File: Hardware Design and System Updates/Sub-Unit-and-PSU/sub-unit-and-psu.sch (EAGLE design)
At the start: 15 parts, among them U1 BA033CC0FP-E2TO252-3_ROM, U2 MSP430FR2000IPW16PW16_TEX, U3 TLR342F-GE2SOP8_ROM, U4 TMP36GT9ZT_3_ADI

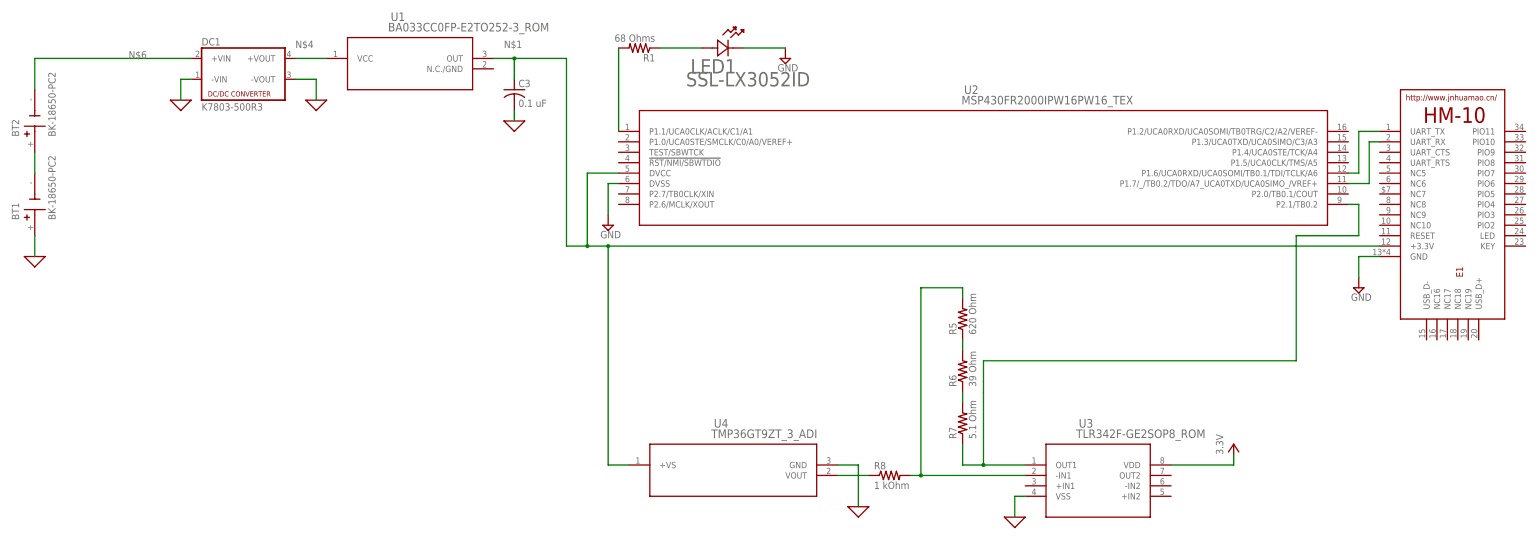
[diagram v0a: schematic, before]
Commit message: Added 5v regulator to schematics
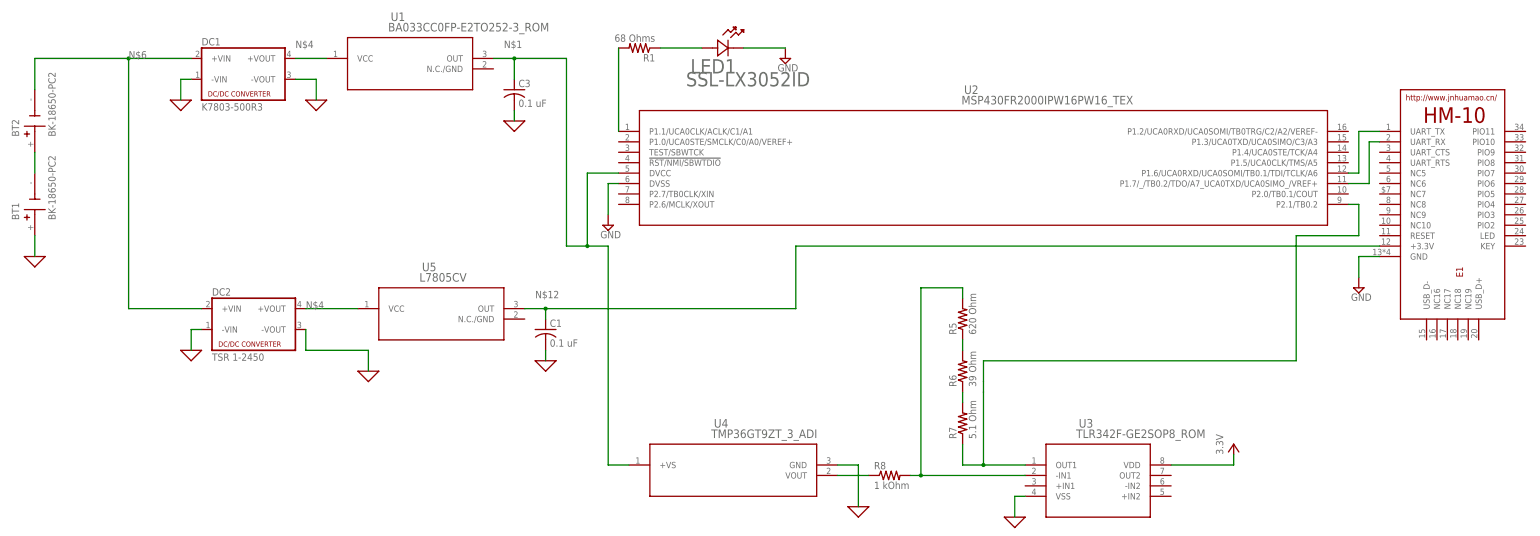
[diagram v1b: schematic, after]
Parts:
- added C1: 0.1 uF, rcl:C-US050-024X044
- added DC2: TSR 1-2450, dc-dc-converter:NME
- added U5: L7805CV, 2023-03-08_12-17-23_Library:BA033CC0FP-E2TO252-3_ROM
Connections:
- new net N$12: C1.1, E1.+3.3V, U5.OUT
- net 0: now also C1.2, DC2.-VIN, DC2.-VOUT
- net N$1: no longer E1.+3.3V
- net N$4: now also DC2.+VOUT, U5.VCC
- net N$6: now also DC2.+VIN
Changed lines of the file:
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@@
 <part name="U4" library="2023-03-28_14-12-25_Library" deviceset="TMP36GT9Z" device="T_3_ADI"/>
 <part name="X_3" library="ngspice-simulation" library_urn="urn:adsk.eagle:library:527439" deviceset="GND" device=""/>
+<part name="DC2" library="dc-dc-converter" library_urn="urn:adsk.eagle:library:208" deviceset="NME" device="" package3d_urn="urn:adsk.eagle:package:12313/1" value="TSR 1-2450"/>
+<part name="X_5" library="ngspice-simulation" library_urn="urn:adsk.eagle:library:527439" deviceset="GND" device=""/>
+<part name="U5" library="2023-03-08_12-17-23_Library" deviceset="BA033CC0FP-E2" device="TO252-3_ROM" value="L7805CV"/>
+<part name="X_8" library="ngspice-simulation" library_urn="urn:adsk.eagle:library:527439" deviceset="GND" device=""/>
+<part name="C1" library="rcl" library_urn="urn:adsk.eagle:library:334" deviceset="C-US" device="050-024X044" package3d_urn="urn:adsk.eagle:package:23643/1" value="0.1 uF"/>
+<part name="X_7" library="ngspice-simulation" library_urn="urn:adsk.eagle:library:527439" deviceset="GND" device=""/>
 </parts>
 <sheets>
@@
 </instance>
 <instance part="X_3" gate="G$1" x="317.5" y="40.64" smashed="yes"/>
+<instance part="DC2" gate="G$1" x="170.18" y="86.36" smashed="yes">
+<attribute name="NAME" x="160.02" y="92.075" size="1.778" layer="95"/>
+<attribute name="VALUE" x="160.02" y="76.2" size="1.778" layer="96"/>
+</instance>
+<instance part="X_5" gate="G$1" x="154.94" y="78.74" smashed="yes"/>
+<instance part="U5" gate="A" x="193.04" y="88.9" smashed="yes">
+<attribute name="NAME" x="211.1746" y="98.0186" size="2.083" layer="95" ratio="6"/>
+<attribute name="VALUE" x="210.5352" y="95.4786" size="2.083" layer="96" ratio="6"/>
+</instance>
+<instance part="X_8" gate="G$1" x="198.12" y="73.66" smashed="yes"/>
+<instance part="C1" gate="G$1" x="241.3" y="83.82" smashed="yes">
+<attribute name="NAME" x="242.316" y="84.455" size="1.778" layer="95"/>
+<attribute name="VALUE" x="242.316" y="79.629" size="1.778" layer="96"/>
+</instance>
+<instance part="X_7" gate="G$1" x="241.3" y="76.2" smashed="yes"/>
 </instances>
 <busses>
@@
 <pinref part="X_3" gate="G$1" pin="0"/>
 </segment>
+<segment>
+<pinref part="X_5" gate="G$1" pin="0"/>
+<pinref part="DC2" gate="G$1" pin="-VIN"/>
+<wire x1="154.94" y1="78.74" x2="154.94" y2="83.82" width="0.1524" layer="91"/>
+<wire x1="154.94" y1="83.82" x2="157.48" y2="83.82" width="0.1524" layer="91"/>
+</segment>
+<segment>
+<pinref part="DC2" gate="G$1" pin="-VOUT"/>
+<wire x1="182.88" y1="83.82" x2="182.88" y2="78.74" width="0.1524" layer="91"/>
+<wire x1="182.88" y1="78.74" x2="198.12" y2="78.74" width="0.1524" layer="91"/>
+<pinref part="X_8" gate="G$1" pin="0"/>
+<wire x1="198.12" y1="73.66" x2="198.12" y2="78.74" width="0.1524" layer="91"/>
+</segment>
+<segment>
+<pinref part="X_7" gate="G$1" pin="0"/>
+<pinref part="C1" gate="G$1" pin="2"/>
+<wire x1="241.3" y1="76.2" x2="241.3" y2="78.74" width="0.1524" layer="91"/>
+</segment>
 </net>
 <net name="N$4" class="0">
@@
 <pinref part="U1" gate="A" pin="VCC"/>
 </segment>
-</net>
-<net name="N$6" class="0">
-<segment>
-<pinref part="DC1" gate="G$1" pin="+VIN"/>
-<wire x1="116.84" y1="149.86" x2="154.94" y2="149.86" width="0.1524" layer="91"/>
-<label x="139.7" y="149.86" size="1.778" layer="95"/>
-<pinref part="BT2" gate="G$1" pin="-"/>
-<wire x1="116.84" y1="142.24" x2="116.84" y2="149.86" width="0.1524" layer="91"/>
+<segment>
+<pinref part="DC2" gate="G$1" pin="+VOUT"/>
+<wire x1="182.88" y1="88.9" x2="195.58" y2="88.9" width="0.1524" layer="91"/>
+<label x="182.88" y="88.9" size="1.778" layer="95"/>
+<pinref part="U5" gate="A" pin="VCC"/>
 </segment>
 </net>
@@
 <wire x1="259.08" y1="121.92" x2="251.46" y2="121.92" width="0.1524" layer="91"/>
 <wire x1="251.46" y1="121.92" x2="251.46" y2="104.14" width="0.1524" layer="91"/>
-<pinref part="E1" gate="G$1" pin="+3.3V"/>
 <wire x1="251.46" y1="104.14" x2="256.54" y2="104.14" width="0.1524" layer="91"/>
 <junction x="251.46" y="104.14"/>
-<wire x1="256.54" y1="104.14" x2="444.5" y2="104.14" width="0.1524" layer="91"/>
 <wire x1="251.46" y1="104.14" x2="246.38" y2="104.14" width="0.1524" layer="91"/>
 <wire x1="228.6" y1="149.86" x2="233.68" y2="149.86" width="0.1524" layer="91"/>
@@
 <wire x1="261.62" y1="50.8" x2="256.54" y2="50.8" width="0.1524" layer="91"/>
 <wire x1="256.54" y1="50.8" x2="256.54" y2="104.14" width="0.1524" layer="91"/>
-<junction x="256.54" y="104.14"/>
 </segment>
 </net>
@@
 </segment>
 </net>
+<net name="N$12" class="0">
+<segment>
+<wire x1="236.22" y1="88.9" x2="241.3" y2="88.9" width="0.1524" layer="91"/>
+<label x="238.76" y="91.44" size="1.778" layer="95"/>
+<pinref part="U5" gate="A" pin="OUT"/>
+<pinref part="C1" gate="G$1" pin="1"/>
+<wire x1="241.3" y1="86.36" x2="241.3" y2="88.9" width="0.1524" layer="91"/>
+<junction x="241.3" y="88.9"/>
+<wire x1="241.3" y1="88.9" x2="302.26" y2="88.9" width="0.1524" layer="91"/>
+<pinref part="E1" gate="G$1" pin="+3.3V"/>
+<wire x1="444.5" y1="104.14" x2="302.26" y2="104.14" width="0.1524" layer="91"/>
+<wire x1="302.26" y1="104.14" x2="302.26" y2="88.9" width="0.1524" layer="91"/>
+</segment>
+</net>
+<net name="N$6" class="0">
+<segment>
+<pinref part="DC2" gate="G$1" pin="+VIN"/>
+<wire x1="139.7" y1="88.9" x2="157.48" y2="88.9" width="0.1524" layer="91"/>
+<pinref part="DC1" gate="G$1" pin="+VIN"/>
+<wire x1="116.84" y1="149.86" x2="139.7" y2="149.86" width="0.1524" layer="91"/>
+<label x="139.7" y="149.86" size="1.778" layer="95"/>
+<pinref part="BT2" gate="G$1" pin="-"/>
+<wire x1="139.7" y1="149.86" x2="154.94" y2="149.86" width="0.1524" layer="91"/>
+<wire x1="116.84" y1="142.24" x2="116.84" y2="149.86" width="0.1524" layer="91"/>
+<wire x1="139.7" y1="88.9" x2="139.7" y2="149.86" width="0.1524" layer="91"/>
+<junction x="139.7" y="149.86"/>
+</segment>
+</net>

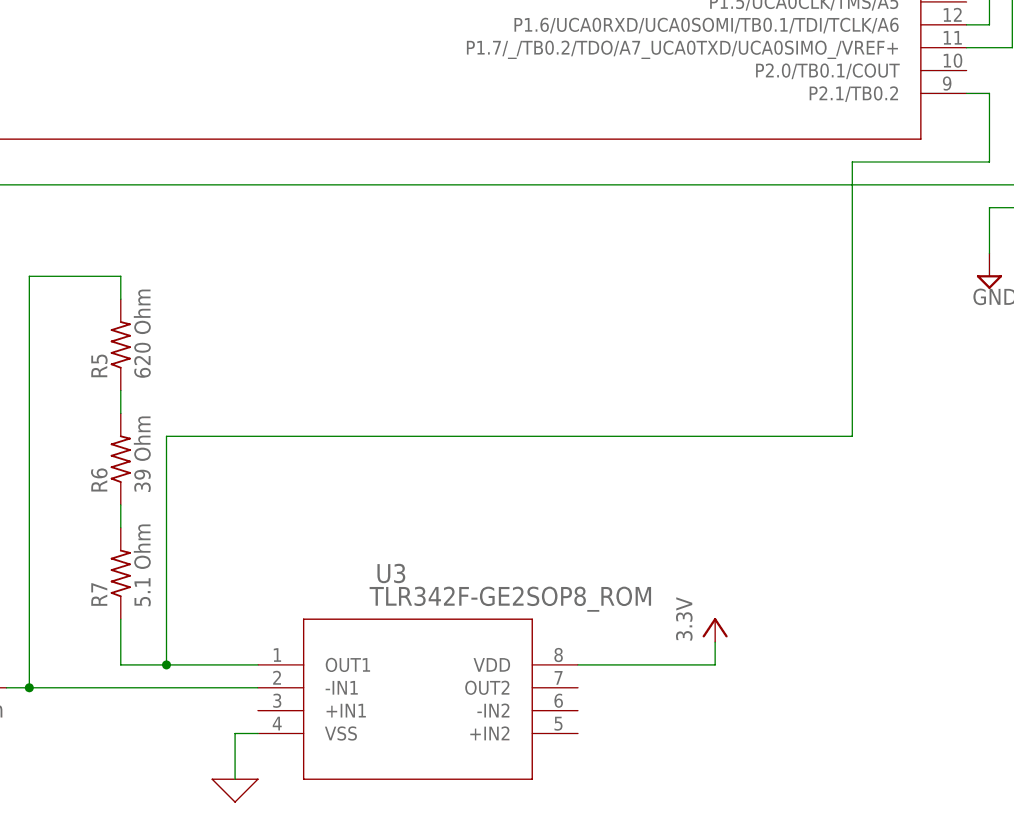
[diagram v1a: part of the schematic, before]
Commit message: Fixed system schematics
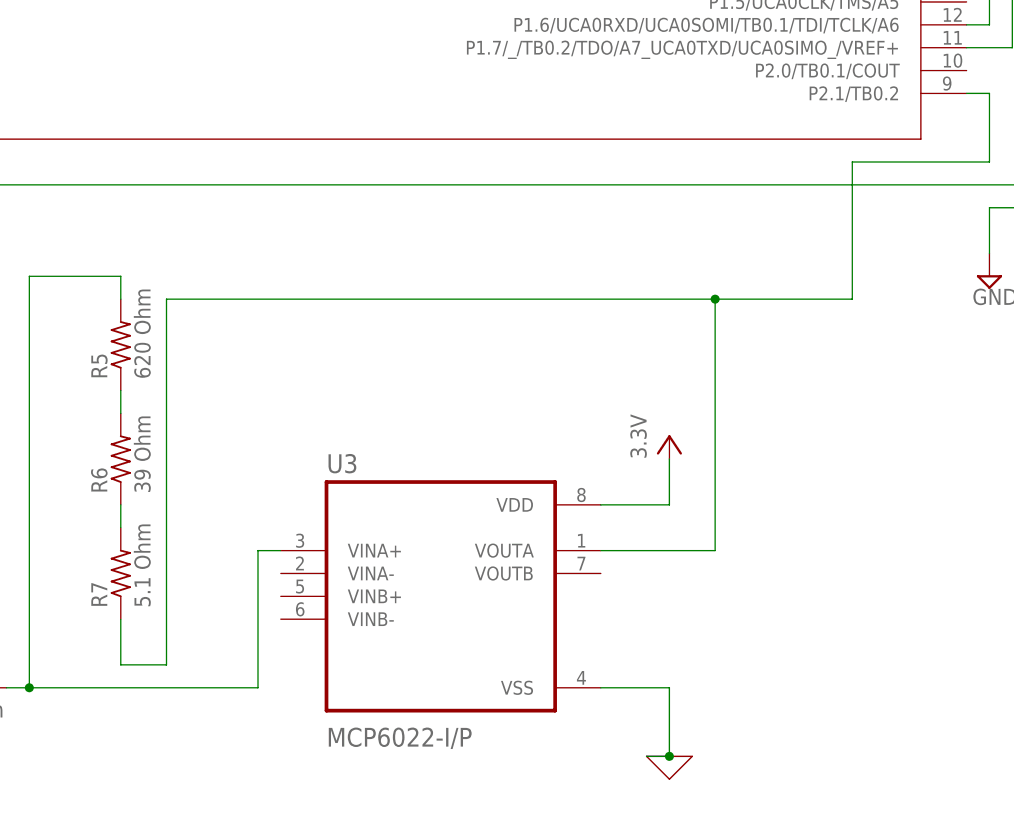
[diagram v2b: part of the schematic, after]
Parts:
- U3: value TLR342F-GE2SOP8_ROM -> MCP6022-I/P; device 2023-03-28_11-48-47_Library:TLR342F-GE2SOP8_ROM -> MCP6022-I_P:MCP6022-I/P
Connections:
- net N$15: now also U3.VOUTA; no longer U3.OUT1
- net N$16: now also U3.VINA+; no longer U3.-IN1
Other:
- moved on the sheet: U3
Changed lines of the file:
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@@
 <part name="SUPPLY1" library="supply2" library_urn="urn:adsk.eagle:library:372" deviceset="GND" device=""/>
 <part name="SUPPLY3" library="supply2" library_urn="urn:adsk.eagle:library:372" deviceset="GND" device=""/>
-<part name="U3" library="2023-03-28_11-48-47_Library" deviceset="TLR342F-GE2" device="SOP8_ROM"/>
 <part name="P+2" library="supply1" library_urn="urn:adsk.eagle:library:371" deviceset="VCC" device="" value="3.3V"/>
 <part name="X_6" library="ngspice-simulation" library_urn="urn:adsk.eagle:library:527439" deviceset="GND" device=""/>
@@
 <part name="C1" library="rcl" library_urn="urn:adsk.eagle:library:334" deviceset="C-US" device="050-024X044" package3d_urn="urn:adsk.eagle:package:23643/1" value="0.1 uF"/>
 <part name="X_7" library="ngspice-simulation" library_urn="urn:adsk.eagle:library:527439" deviceset="GND" device=""/>
+<part name="U3" library="MCP6022-I_P" deviceset="MCP6022-I/P" device=""/>
 </parts>
 <sheets>
@@
 <attribute name="VALUE" x="254.635" y="106.045" size="1.778" layer="96"/>
 </instance>
-<instance part="U3" gate="A" x="355.6" y="50.8" smashed="yes">
-<attribute name="NAME" x="371.1946" y="59.9186" size="2.083" layer="95" ratio="6"/>
-<attribute name="VALUE" x="370.5552" y="57.3786" size="2.083" layer="96" ratio="6"/>
-</instance>
-<instance part="P+2" gate="VCC" x="408.94" y="55.88" smashed="yes">
-<attribute name="VALUE" x="406.4" y="53.34" size="1.778" layer="96" rot="R90"/>
-</instance>
-<instance part="X_6" gate="G$1" x="355.6" y="38.1" smashed="yes"/>
+<instance part="P+2" gate="VCC" x="403.86" y="76.2" smashed="yes">
+<attribute name="VALUE" x="401.32" y="73.66" size="1.778" layer="96" rot="R90"/>
+</instance>
+<instance part="X_6" gate="G$1" x="403.86" y="40.64" smashed="yes"/>
 <instance part="R5" gate="G$1" x="342.9" y="86.36" smashed="yes" rot="R90">
 <attribute name="NAME" x="341.4014" y="82.55" size="1.778" layer="95" rot="R90"/>
@@
 </instance>
 <instance part="X_7" gate="G$1" x="241.3" y="76.2" smashed="yes"/>
+<instance part="U3" gate="A" x="378.46" y="58.42" smashed="yes">
+<attribute name="NAME" x="365.76" y="72.12" size="2.0828" layer="95" ratio="10" rot="SR0"/>
+<attribute name="VALUE" x="365.76" y="41.72" size="2.0828" layer="96" ratio="10" rot="SR0"/>
+</instance>
 </instances>
 <busses>
@@
 </segment>
 <segment>
-<pinref part="X_6" gate="G$1" pin="0"/>
-<pinref part="U3" gate="A" pin="VSS"/>
-<wire x1="355.6" y1="38.1" x2="355.6" y2="43.18" width="0.1524" layer="91"/>
-<wire x1="355.6" y1="43.18" x2="358.14" y2="43.18" width="0.1524" layer="91"/>
-</segment>
-<segment>
 <pinref part="U4" gate="A" pin="GND"/>
 <wire x1="312.42" y1="50.8" x2="317.5" y2="50.8" width="0.1524" layer="91"/>
@@
 <pinref part="C1" gate="G$1" pin="2"/>
 <wire x1="241.3" y1="76.2" x2="241.3" y2="78.74" width="0.1524" layer="91"/>
+</segment>
+<segment>
+<wire x1="401.32" y1="40.64" x2="403.86" y2="40.64" width="0.1524" layer="91"/>
+<wire x1="403.86" y1="40.64" x2="403.86" y2="48.26" width="0.1524" layer="91"/>
+<pinref part="U3" gate="A" pin="VSS"/>
+<wire x1="403.86" y1="48.26" x2="396.24" y2="48.26" width="0.1524" layer="91"/>
+<pinref part="X_6" gate="G$1" pin="0"/>
+<junction x="403.86" y="40.64"/>
 </segment>
 </net>
@@
 </segment>
 </net>
-<net name="VCC" class="0">
-<segment>
-<pinref part="U3" gate="A" pin="VDD"/>
-<wire x1="393.7" y1="50.8" x2="408.94" y2="50.8" width="0.1524" layer="91"/>
-<pinref part="P+2" gate="VCC" pin="VCC"/>
-<wire x1="408.94" y1="50.8" x2="408.94" y2="53.34" width="0.1524" layer="91"/>
-</segment>
-</net>
 <net name="N$13" class="0">
 <segment>
@@
 <net name="N$15" class="0">
 <segment>
-<pinref part="U3" gate="A" pin="OUT1"/>
-<wire x1="358.14" y1="50.8" x2="347.98" y2="50.8" width="0.1524" layer="91"/>
 <pinref part="R7" gate="G$1" pin="1"/>
 <wire x1="347.98" y1="50.8" x2="342.9" y2="50.8" width="0.1524" layer="91"/>
 <wire x1="342.9" y1="50.8" x2="342.9" y2="55.88" width="0.1524" layer="91"/>
-<wire x1="347.98" y1="50.8" x2="347.98" y2="68.58" width="0.1524" layer="91"/>
-<junction x="347.98" y="50.8"/>
+<wire x1="347.98" y1="50.8" x2="347.98" y2="91.44" width="0.1524" layer="91"/>
 <pinref part="U2" gate="A" pin="P2.1/TB0.2"/>
-<wire x1="347.98" y1="68.58" x2="347.98" y2="71.12" width="0.1524" layer="91"/>
 <wire x1="436.88" y1="114.3" x2="439.42" y2="114.3" width="0.1524" layer="91"/>
 <wire x1="439.42" y1="114.3" x2="439.42" y2="106.68" width="0.1524" layer="91"/>
 <wire x1="439.42" y1="106.68" x2="424.18" y2="106.68" width="0.1524" layer="91"/>
-<wire x1="424.18" y1="106.68" x2="424.18" y2="76.2" width="0.1524" layer="91"/>
-<wire x1="424.18" y1="76.2" x2="347.98" y2="76.2" width="0.1524" layer="91"/>
-<wire x1="347.98" y1="76.2" x2="347.98" y2="71.12" width="0.1524" layer="91"/>
+<wire x1="424.18" y1="106.68" x2="424.18" y2="91.44" width="0.1524" layer="91"/>
+<wire x1="424.18" y1="91.44" x2="408.94" y2="91.44" width="0.1524" layer="91"/>
+<pinref part="U3" gate="A" pin="VOUTA"/>
+<wire x1="408.94" y1="91.44" x2="347.98" y2="91.44" width="0.1524" layer="91"/>
+<wire x1="396.24" y1="63.5" x2="408.94" y2="63.5" width="0.1524" layer="91"/>
+<wire x1="408.94" y1="63.5" x2="408.94" y2="91.44" width="0.1524" layer="91"/>
+<junction x="408.94" y="91.44"/>
 </segment>
 </net>
@@
 <wire x1="342.9" y1="91.44" x2="342.9" y2="93.98" width="0.1524" layer="91"/>
 <wire x1="342.9" y1="93.98" x2="332.74" y2="93.98" width="0.1524" layer="91"/>
-<pinref part="U3" gate="A" pin="-IN1"/>
 <wire x1="358.14" y1="48.26" x2="332.74" y2="48.26" width="0.1524" layer="91"/>
 <pinref part="R8" gate="G$1" pin="2"/>
@@
 <wire x1="332.74" y1="93.98" x2="332.74" y2="48.26" width="0.1524" layer="91"/>
 <junction x="332.74" y="48.26"/>
+<wire x1="358.14" y1="48.26" x2="358.14" y2="63.5" width="0.1524" layer="91"/>
+<pinref part="U3" gate="A" pin="VINA+"/>
+<wire x1="358.14" y1="63.5" x2="360.68" y2="63.5" width="0.1524" layer="91"/>
 </segment>
 </net>
@@
 </segment>
 </net>
+<net name="VCC" class="0">
+<segment>
+<pinref part="U3" gate="A" pin="VDD"/>
+<wire x1="396.24" y1="68.58" x2="403.86" y2="68.58" width="0.1524" layer="91"/>
+<pinref part="P+2" gate="VCC" pin="VCC"/>
+<wire x1="403.86" y1="68.58" x2="403.86" y2="73.66" width="0.1524" layer="91"/>
+</segment>
+</net>
